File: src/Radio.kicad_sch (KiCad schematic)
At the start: 12 parts, among them J17 Line out, Q5 BPW96B

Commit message: Update Schematics design
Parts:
- removed Q5: BPW96B, LED_THT:LED_D5.0mm, symbol Device:Q_Photo_NPN
- renumbered J17 to J26
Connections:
- net GND: no longer J?.4 (Pin_4)
- net LightSensor: no longer names the net of J?.3 (Pin_3)
- new net GNDRadio: J?.4 (Pin_4)
- no-connect marks 0 -> 1
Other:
- note added: "Crashbar speakers"
- note added: "Handlebar speakers"
- note added: "Left Side Fork Column cover"
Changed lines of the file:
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@@
   (junction (at 255.27 111.76) (diameter 0) (color 0 0 0 0)
   )
-  (junction (at 142.24 85.09) (diameter 0) (color 0 0 0 0)
-  )
   (junction (at 97.79 76.2) (diameter 0) (color 0 0 0 0)
   )
-  (junction (at 129.54 67.31) (diameter 0) (color 0 0 0 0)
-  )
-  (wire (pts (xy 129.54 85.09) (xy 142.24 85.09))
-    (stroke (width 0) (type default))
-  )
+  (no_connect (at 142.24 67.31))
   (wire (pts (xy 238.76 116.84) (xy 228.6 116.84))
     (stroke (width 0) (type default) (color 72 72 72 1))
@@
     (stroke (width 0) (type default))
   )
-  (wire (pts (xy 142.24 69.85) (xy 142.24 85.09))
+  (wire (pts (xy 142.24 69.85) (xy 142.24 101.6))
     (stroke (width 0) (type default))
   )
@@
   )
   (wire (pts (xy 54.61 76.2) (xy 54.61 72.39))
-    (stroke (width 0) (type default))
-  )
-  (wire (pts (xy 142.24 85.09) (xy 142.24 101.6))
     (stroke (width 0) (type default))
   )
@@
     (stroke (width 0) (type default) (color 255 255 255 1))
   )
-  (wire (pts (xy 129.54 85.09) (xy 129.54 81.28))
-    (stroke (width 0) (type default))
-  )
   (wire (pts (xy 54.61 100.33) (xy 69.85 100.33))
     (stroke (width 0) (type default))
   )
-  (wire (pts (xy 125.73 67.31) (xy 129.54 67.31))
-    (stroke (width 0) (type default))
-  )
   (wire (pts (xy 144.78 137.16) (xy 147.32 137.16))
     (stroke (width 0) (type default))
@@
   )
   (wire (pts (xy 48.26 127) (xy 54.61 127))
-    (stroke (width 0) (type default))
-  )
-  (wire (pts (xy 129.54 67.31) (xy 142.24 67.31))
     (stroke (width 0) (type default))
   )
@@
     (stroke (width 0) (type default))
   )
-  (wire (pts (xy 129.54 71.12) (xy 129.54 67.31))
-    (stroke (width 0) (type default))
-  )
   (wire (pts (xy 246.38 105.41) (xy 228.6 105.41))
     (stroke (width 0) (type default))
@@
     (fill (type none))
   )
+  (rectangle (start 243.84 91.44) (end 267.97 146.05)
+    (stroke (width 0) (type default))
+    (fill (type none))
+  )
   (text "Speakers" (at 38.1 63.5 0)
+    (effects (font (size 1.27 1.27)) (justify left bottom))
+  )
+  (text "Handlebar speakers" (at 67.31 71.12 0)
+    (effects (font (size 1.27 1.27)) (justify left bottom))
+  )
+  (text "Left Side Fork Column cover" (at 243.84 148.59 0)
+    (effects (font (size 1.27 1.27)) (justify left bottom))
+  )
+  (text "Crashbar speakers" (at 67.31 133.35 0)
     (effects (font (size 1.27 1.27)) (justify left bottom))
   )
@@
     (effects (font (size 1.27 1.27)) (justify right))
     (property "Intersheetrefs" "${INTERSHEET_REFS}" (at 218.7168 102.87 0)
-      (effects (font (size 1.27 1.27)) (justify right) hide)
-    )
-  )
-  (global_label "LightSensor" (shape output) (at 125.73 67.31 180) (fields_autoplaced)
-    (effects (font (size 1.27 1.27)) (justify right))
-    (property "Intersheetrefs" "${INTERSHEET_REFS}" (at 111.7572 67.31 0)
       (effects (font (size 1.27 1.27)) (justify right) hide)
     )
@@
         )
         (path "/e63e39d7-6ac0-4ffd-8aa3-1841a4541b55/ddab4412-d22a-447e-a3b8-944a9a68a530"
-          (reference "J13") (unit 1)
-        )
-      )
-    )
-  )
-  (symbol (lib_id "power:GND") (at 176.53 101.6 90) (unit 1)
-    (in_bom yes) (on_board yes) (dnp no)
-    (property "Reference" "#PWR?" (at 182.88 101.6 0)
-      (effects (font (size 1.27 1.27)) hide)
-    )
-    (property "Value" "GND" (at 180.34 101.6 90)
-      (effects (font (size 1.27 1.27)) (justify right))
-    )
-    (property "Footprint" "" (at 176.53 101.6 0)
-      (effects (font (size 1.27 1.27)) hide)
-    )
-    (property "Datasheet" "" (at 176.53 101.6 0)
-      (effects (font (size 1.27 1.27)) hide)
-    )
-    (pin "1")
-    (instances
-      (project "dragstar-infotainment"
-        (path "/e63e39d7-6ac0-4ffd-8aa3-1841a4541b55"
-          (reference "#PWR?") (unit 1)
-        )
-        (path "/e63e39d7-6ac0-4ffd-8aa3-1841a4541b55/ddab4412-d22a-447e-a3b8-944a9a68a530"
-          (reference "#PWR068") (unit 1)
+          (reference "J22") (unit 1)
         )
       )
@@
         )
         (path "/e63e39d7-6ac0-4ffd-8aa3-1841a4541b55/ddab4412-d22a-447e-a3b8-944a9a68a530"
-          (reference "J15") (unit 1)
+          (reference "J24") (unit 1)
         )
       )
@@
         )
         (path "/e63e39d7-6ac0-4ffd-8aa3-1841a4541b55/ddab4412-d22a-447e-a3b8-944a9a68a530"
-          (reference "#PWR071") (unit 1)
+          (reference "#PWR074") (unit 1)
         )
       )
@@
         )
         (path "/e63e39d7-6ac0-4ffd-8aa3-1841a4541b55/ddab4412-d22a-447e-a3b8-944a9a68a530"
-          (reference "J11") (unit 1)
+          (reference "J20") (unit 1)
         )
       )
@@
         )
         (path "/e63e39d7-6ac0-4ffd-8aa3-1841a4541b55/ddab4412-d22a-447e-a3b8-944a9a68a530"
-          (reference "J14") (unit 1)
+          (reference "J23") (unit 1)
         )
       )
@@
         )
         (path "/e63e39d7-6ac0-4ffd-8aa3-1841a4541b55/ddab4412-d22a-447e-a3b8-944a9a68a530"
-          (reference "#PWR073") (unit 1)
+          (reference "#PWR076") (unit 1)
         )
       )
@@
         (path "/e63e39d7-6ac0-4ffd-8aa3-1841a4541b55/ddab4412-d22a-447e-a3b8-944a9a68a530"
           (reference "LS4") (unit 1)
+        )
+      )
+    )
+  )
+  (symbol (lib_id "Local Components:GNDRadio") (at 176.53 101.6 90) (unit 1)
+    (in_bom yes) (on_board yes) (dnp no) (fields_autoplaced)
+    (property "Reference" "#PWR021" (at 182.88 101.6 0)
+      (effects (font (size 1.27 1.27)) hide)
+    )
+    (property "Value" "GNDRadio" (at 180.34 102.235 90)
+      (effects (font (size 1.27 1.27)) (justify right))
+    )
+    (property "Footprint" "" (at 176.53 101.6 0)
+      (effects (font (size 1.27 1.27)) hide)
+    )
+    (property "Datasheet" "" (at 176.53 101.6 0)
+      (effects (font (size 1.27 1.27)) hide)
+    )
+    (pin "1")
+    (instances
+      (project "dragstar-infotainment"
+        (path "/e63e39d7-6ac0-4ffd-8aa3-1841a4541b55/5d40715c-dfc9-4b95-9cc7-adbd4b609d9b"
+          (reference "#PWR021") (unit 1)
+        )
+        (path "/e63e39d7-6ac0-4ffd-8aa3-1841a4541b55/ddab4412-d22a-447e-a3b8-944a9a68a530"
+          (reference "#PWR071") (unit 1)
         )
       )
@@
         )
         (path "/e63e39d7-6ac0-4ffd-8aa3-1841a4541b55/ddab4412-d22a-447e-a3b8-944a9a68a530"
-          (reference "J12") (unit 1)
+          (reference "J21") (unit 1)
         )
       )
@@
   (symbol (lib_id "Local Components:+5VRadio") (at 228.6 97.79 90) (unit 1)
     (in_bom yes) (on_board yes) (dnp no)
-    (property "Reference" "#PWR070" (at 232.41 97.79 0)
+    (property "Reference" "#PWR073" (at 232.41 97.79 0)
       (effects (font (size 1.27 1.27)) hide)
     )
@@
       (project "dragstar-infotainment"
         (path "/e63e39d7-6ac0-4ffd-8aa3-1841a4541b55/ddab4412-d22a-447e-a3b8-944a9a68a530"
-          (reference "#PWR070") (unit 1)
+          (reference "#PWR073") (unit 1)
         )
       )
@@
         )
         (path "/e63e39d7-6ac0-4ffd-8aa3-1841a4541b55/ddab4412-d22a-447e-a3b8-944a9a68a530"
-          (reference "#PWR072") (unit 1)
+          (reference "#PWR075") (unit 1)
         )
       )
@@
         )
         (path "/e63e39d7-6ac0-4ffd-8aa3-1841a4541b55/ddab4412-d22a-447e-a3b8-944a9a68a530"
-          (reference "#PWR069") (unit 1)
+          (reference "#PWR072") (unit 1)
         )
       )
@@
   (symbol (lib_id "Connector:Conn_Coaxial_x2") (at 255.27 119.38 0) (unit 1)
     (in_bom yes) (on_board yes) (dnp no) (fields_autoplaced)
-    (property "Reference" "J17" (at 257.81 119.0382 0)
+    (property "Reference" "J26" (at 257.81 119.0382 0)
       (effects (font (size 1.27 1.27)) (justify left))
     )
@@
       (project "dragstar-infotainment"
         (path "/e63e39d7-6ac0-4ffd-8aa3-1841a4541b55/ddab4412-d22a-447e-a3b8-944a9a68a530"
-          (reference "J17") (unit 1)
+          (reference "J26") (unit 1)
         )
       )
@@
         )
         (path "/e63e39d7-6ac0-4ffd-8aa3-1841a4541b55/ddab4412-d22a-447e-a3b8-944a9a68a530"
-          (reference "J16") (unit 1)
-        )
-      )
-    )
-  )
-  (symbol (lib_id "Device:Q_Photo_NPN") (at 127 76.2 0) (unit 1)
-    (in_bom yes) (on_board yes) (dnp no)
-    (property "Reference" "Q5" (at 132.08 74.8157 0)
-      (effects (font (size 1.27 1.27)) (justify left))
-    )
-    (property "Value" "BPW96B" (at 120.65 81.28 0)
-      (effects (font (size 1.27 1.27)) (justify left))
-    )
-    (property "Footprint" "LED_THT:LED_D5.0mm" (at 132.08 73.66 0)
-      (effects (font (size 1.27 1.27)) hide)
-    )
-    (property "Datasheet" "https://storage.googleapis.com/mauser-public-files/mauser.pt/catalog/userfiles/bpw96.pdf" (at 127 76.2 0)
-      (effects (font (size 1.27 1.27)) hide)
-    )
-    (property "Vendor" "Mauser" (at 127 76.2 0)
-      (effects (font (size 1.27 1.27)) hide)
-    )
-    (property "Vendor Link" "https://mauser.pt/catalog/product_info.php?products_id=017-0313" (at 127 76.2 0)
-      (effects (font (size 1.27 1.27)) hide)
-    )
-    (property "Vendor Ref" "017-0313" (at 127 76.2 0)
-      (effects (font (size 1.27 1.27)) hide)
-    )
-    (pin "1")
-    (pin "2")
-    (instances
-      (project "dragstar-infotainment"
-        (path "/e63e39d7-6ac0-4ffd-8aa3-1841a4541b55/ddab4412-d22a-447e-a3b8-944a9a68a530"
-          (reference "Q5") (unit 1)
+          (reference "J25") (unit 1)
         )
       )
@@
         )
         (path "/e63e39d7-6ac0-4ffd-8aa3-1841a4541b55/ddab4412-d22a-447e-a3b8-944a9a68a530"
-          (reference "#FLG012") (unit 1)
+          (reference "#FLG013") (unit 1)
         )
       )
@@
         )
         (path "/e63e39d7-6ac0-4ffd-8aa3-1841a4541b55/ddab4412-d22a-447e-a3b8-944a9a68a530"
-          (reference "#PWR067") (unit 1)
-        )
-      )
+          (reference "#PWR070") (unit 1)
+        )
+      )

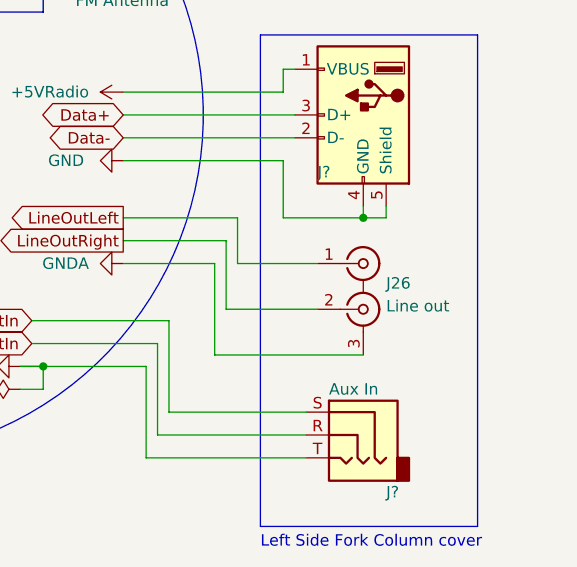
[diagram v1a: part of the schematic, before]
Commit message: Add radio backup battery circuit; Update cable harness; rework main board circuit
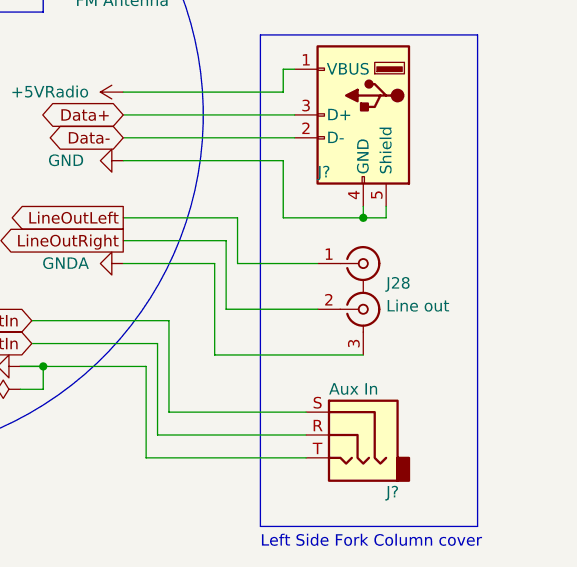
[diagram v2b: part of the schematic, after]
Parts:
- renumbered J26 to J28
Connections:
- net VRadio: no longer J?.1 (VBUS)
- new net +5VRadio: J?.1 (VBUS)
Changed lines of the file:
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@@
   )
   (wire (pts (xy 246.38 97.79) (xy 246.38 95.25))
-    (stroke (width 0) (type default) (color 255 0 0 1))
+    (stroke (width 0) (type default))
   )
   (wire (pts (xy 97.79 127) (xy 104.14 127))
@@
   )
   (wire (pts (xy 246.38 95.25) (xy 247.65 95.25))
-    (stroke (width 0) (type default) (color 255 0 0 1))
+    (stroke (width 0) (type default))
   )
   (wire (pts (xy 238.76 127) (xy 238.76 116.84))
@@
   )
   (wire (pts (xy 228.6 97.79) (xy 246.38 97.79))
-    (stroke (width 0) (type default) (color 255 0 0 1))
+    (stroke (width 0) (type default))
   )
   (wire (pts (xy 95.25 76.2) (xy 88.9 76.2))
@@
         )
         (path "/e63e39d7-6ac0-4ffd-8aa3-1841a4541b55/ddab4412-d22a-447e-a3b8-944a9a68a530"
-          (reference "J22") (unit 1)
+          (reference "J24") (unit 1)
         )
       )
@@
         )
         (path "/e63e39d7-6ac0-4ffd-8aa3-1841a4541b55/ddab4412-d22a-447e-a3b8-944a9a68a530"
-          (reference "J24") (unit 1)
+          (reference "J26") (unit 1)
         )
       )
@@
         )
         (path "/e63e39d7-6ac0-4ffd-8aa3-1841a4541b55/ddab4412-d22a-447e-a3b8-944a9a68a530"
-          (reference "#PWR074") (unit 1)
+          (reference "#PWR075") (unit 1)
         )
       )
@@
         )
         (path "/e63e39d7-6ac0-4ffd-8aa3-1841a4541b55/ddab4412-d22a-447e-a3b8-944a9a68a530"
-          (reference "J20") (unit 1)
+          (reference "J22") (unit 1)
         )
       )
@@
         )
         (path "/e63e39d7-6ac0-4ffd-8aa3-1841a4541b55/ddab4412-d22a-447e-a3b8-944a9a68a530"
-          (reference "J23") (unit 1)
+          (reference "J25") (unit 1)
         )
       )
@@
         )
         (path "/e63e39d7-6ac0-4ffd-8aa3-1841a4541b55/ddab4412-d22a-447e-a3b8-944a9a68a530"
-          (reference "#PWR076") (unit 1)
+          (reference "#PWR077") (unit 1)
         )
       )
@@
   (symbol (lib_id "Local Components:GNDRadio") (at 176.53 101.6 90) (unit 1)
     (in_bom yes) (on_board yes) (dnp no) (fields_autoplaced)
-    (property "Reference" "#PWR021" (at 182.88 101.6 0)
+    (property "Reference" "#PWR?" (at 182.88 101.6 0)
       (effects (font (size 1.27 1.27)) hide)
     )
@@
       (project "dragstar-infotainment"
         (path "/e63e39d7-6ac0-4ffd-8aa3-1841a4541b55/5d40715c-dfc9-4b95-9cc7-adbd4b609d9b"
-          (reference "#PWR021") (unit 1)
-        )
-        (path "/e63e39d7-6ac0-4ffd-8aa3-1841a4541b55/ddab4412-d22a-447e-a3b8-944a9a68a530"
-          (reference "#PWR071") (unit 1)
+          (reference "#PWR?") (unit 1)
+        )
+        (path "/e63e39d7-6ac0-4ffd-8aa3-1841a4541b55/ddab4412-d22a-447e-a3b8-944a9a68a530"
+          (reference "#PWR072") (unit 1)
+        )
+      )
+    )
+  )
+  (symbol (lib_id "Local Components:+5VRadio") (at 228.6 97.79 90) (unit 1)
+    (in_bom yes) (on_board yes) (dnp no)
+    (property "Reference" "#PWR074" (at 232.41 97.79 0)
+      (effects (font (size 1.27 1.27)) hide)
+    )
+    (property "Value" "+5VRadio" (at 224.79 97.79 90)
+      (effects (font (size 1.27 1.27)) (justify left))
+    )
+    (property "Footprint" "" (at 228.6 97.79 0)
+      (effects (font (size 1.27 1.27)) hide)
+    )
+    (property "Datasheet" "" (at 228.6 97.79 0)
+      (effects (font (size 1.27 1.27)) hide)
+    )
+    (pin "1")
+    (instances
+      (project "dragstar-infotainment"
+        (path "/e63e39d7-6ac0-4ffd-8aa3-1841a4541b55/ddab4412-d22a-447e-a3b8-944a9a68a530"
+          (reference "#PWR074") (unit 1)
         )
       )
@@
         )
         (path "/e63e39d7-6ac0-4ffd-8aa3-1841a4541b55/ddab4412-d22a-447e-a3b8-944a9a68a530"
-          (reference "J21") (unit 1)
-        )
-      )
-    )
-  )
-  (symbol (lib_id "Local Components:+5VRadio") (at 228.6 97.79 90) (unit 1)
-    (in_bom yes) (on_board yes) (dnp no)
-    (property "Reference" "#PWR073" (at 232.41 97.79 0)
-      (effects (font (size 1.27 1.27)) hide)
-    )
-    (property "Value" "+5VRadio" (at 224.79 97.79 90)
-      (effects (font (size 1.27 1.27)) (justify left))
-    )
-    (property "Footprint" "" (at 228.6 97.79 0)
-      (effects (font (size 1.27 1.27)) hide)
-    )
-    (property "Datasheet" "" (at 228.6 97.79 0)
-      (effects (font (size 1.27 1.27)) hide)
-    )
-    (pin "1")
-    (instances
-      (project "dragstar-infotainment"
-        (path "/e63e39d7-6ac0-4ffd-8aa3-1841a4541b55/ddab4412-d22a-447e-a3b8-944a9a68a530"
-          (reference "#PWR073") (unit 1)
+          (reference "J23") (unit 1)
         )
       )
@@
         )
         (path "/e63e39d7-6ac0-4ffd-8aa3-1841a4541b55/ddab4412-d22a-447e-a3b8-944a9a68a530"
-          (reference "#PWR075") (unit 1)
+          (reference "#PWR076") (unit 1)
         )
       )
@@
         )
         (path "/e63e39d7-6ac0-4ffd-8aa3-1841a4541b55/ddab4412-d22a-447e-a3b8-944a9a68a530"
-          (reference "#PWR072") (unit 1)
+          (reference "#PWR073") (unit 1)
         )
       )
@@
   (symbol (lib_id "Connector:Conn_Coaxial_x2") (at 255.27 119.38 0) (unit 1)
     (in_bom yes) (on_board yes) (dnp no) (fields_autoplaced)
-    (property "Reference" "J26" (at 257.81 119.0382 0)
+    (property "Reference" "J28" (at 257.81 119.0382 0)
       (effects (font (size 1.27 1.27)) (justify left))
     )
@@
       (project "dragstar-infotainment"
         (path "/e63e39d7-6ac0-4ffd-8aa3-1841a4541b55/ddab4412-d22a-447e-a3b8-944a9a68a530"
-          (reference "J26") (unit 1)
+          (reference "J28") (unit 1)
         )
       )
@@
         )
         (path "/e63e39d7-6ac0-4ffd-8aa3-1841a4541b55/ddab4412-d22a-447e-a3b8-944a9a68a530"
-          (reference "J25") (unit 1)
+          (reference "J27") (unit 1)
         )
       )
@@
         )
         (path "/e63e39d7-6ac0-4ffd-8aa3-1841a4541b55/ddab4412-d22a-447e-a3b8-944a9a68a530"
-          (reference "#FLG013") (unit 1)
+          (reference "#FLG012") (unit 1)
         )
       )
@@
         )
         (path "/e63e39d7-6ac0-4ffd-8aa3-1841a4541b55/ddab4412-d22a-447e-a3b8-944a9a68a530"
-          (reference "#PWR070") (unit 1)
-        )
-      )
+          (reference "#PWR071") (unit 1)
+        )
+      )

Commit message: update Schematics
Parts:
- removed J28: Line out, symbol Connector:Conn_Coaxial_x2
- added AE1: Antenna_Shield, symbol Device:Antenna_Shield
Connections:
- net GNDRadio is gone; now on net GND: J?.4 (Pin_4)
- net GND: now also AE1.2 (Shield)
- net Ant: no longer names the net of J?.1 (In)
- net Ant: now also AE1.1 (A)
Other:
- moved on the sheet: J?

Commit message: Update Schmatics; Cleanup unecessary circuits; Simplify blinkers dimmers; Update PCB; Colorize motorcycle electric diagram.
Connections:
- net Killswitch renamed Key
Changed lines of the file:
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@@
     )
   )
-  (global_label "Killswitch" (shape output) (at 177.8 96.52 0) (fields_autoplaced)
+  (global_label "Key" (shape output) (at 177.8 96.52 0) (fields_autoplaced)
     (effects (font (size 1.27 1.27)) (justify left))
-    (property "Intersheetrefs" "${INTERSHEET_REFS}" (at 189.8377 96.52 0)
+    (property "Intersheetrefs" "${INTERSHEET_REFS}" (at 184.032 96.52 0)
       (effects (font (size 1.27 1.27)) (justify left) hide)
     )
@@
         )
         (path "/e63e39d7-6ac0-4ffd-8aa3-1841a4541b55/ddab4412-d22a-447e-a3b8-944a9a68a530"
-          (reference "J13") (unit 1)
+          (reference "J47") (unit 1)
         )
       )
@@
         )
         (path "/e63e39d7-6ac0-4ffd-8aa3-1841a4541b55/ddab4412-d22a-447e-a3b8-944a9a68a530"
-          (reference "J12") (unit 1)
+          (reference "J49") (unit 1)
         )
       )
@@
         )
         (path "/e63e39d7-6ac0-4ffd-8aa3-1841a4541b55/ddab4412-d22a-447e-a3b8-944a9a68a530"
-          (reference "LS1") (unit 1)
+          (reference "LS2") (unit 1)
         )
       )
@@
         )
         (path "/e63e39d7-6ac0-4ffd-8aa3-1841a4541b55/ddab4412-d22a-447e-a3b8-944a9a68a530"
-          (reference "#PWR058") (unit 1)
+          (reference "#PWR070") (unit 1)
         )
       )
@@
         )
         (path "/e63e39d7-6ac0-4ffd-8aa3-1841a4541b55/ddab4412-d22a-447e-a3b8-944a9a68a530"
-          (reference "#FLG010") (unit 1)
+          (reference "#FLG011") (unit 1)
         )
       )
@@
         )
         (path "/e63e39d7-6ac0-4ffd-8aa3-1841a4541b55/ddab4412-d22a-447e-a3b8-944a9a68a530"
-          (reference "J10") (unit 1)
+          (reference "J45") (unit 1)
         )
       )
@@
         )
         (path "/e63e39d7-6ac0-4ffd-8aa3-1841a4541b55/ddab4412-d22a-447e-a3b8-944a9a68a530"
-          (reference "J9") (unit 1)
+          (reference "J48") (unit 1)
         )
       )
@@
         )
         (path "/e63e39d7-6ac0-4ffd-8aa3-1841a4541b55/ddab4412-d22a-447e-a3b8-944a9a68a530"
-          (reference "#PWR054") (unit 1)
+          (reference "#PWR071") (unit 1)
         )
       )
@@
         )
         (path "/e63e39d7-6ac0-4ffd-8aa3-1841a4541b55/ddab4412-d22a-447e-a3b8-944a9a68a530"
-          (reference "LS3") (unit 1)
+          (reference "LS1") (unit 1)
         )
       )
@@
   (symbol (lib_id "Local Components:+5VRadio") (at 228.6 97.79 90) (unit 1)
     (in_bom yes) (on_board yes) (dnp no)
-    (property "Reference" "#PWR055" (at 232.41 97.79 0)
+    (property "Reference" "#PWR069" (at 232.41 97.79 0)
       (effects (font (size 1.27 1.27)) hide)
     )
@@
       (project "dragstar-infotainment"
         (path "/e63e39d7-6ac0-4ffd-8aa3-1841a4541b55/ddab4412-d22a-447e-a3b8-944a9a68a530"
-          (reference "#PWR055") (unit 1)
+          (reference "#PWR069") (unit 1)
         )
       )
@@
         )
         (path "/e63e39d7-6ac0-4ffd-8aa3-1841a4541b55/ddab4412-d22a-447e-a3b8-944a9a68a530"
-          (reference "J8") (unit 1)
+          (reference "J46") (unit 1)
         )
       )
@@
         )
         (path "/e63e39d7-6ac0-4ffd-8aa3-1841a4541b55/ddab4412-d22a-447e-a3b8-944a9a68a530"
-          (reference "#PWR059") (unit 1)
+          (reference "#PWR068") (unit 1)
         )
       )
@@
         )
         (path "/e63e39d7-6ac0-4ffd-8aa3-1841a4541b55/ddab4412-d22a-447e-a3b8-944a9a68a530"
-          (reference "J11") (unit 1)
+          (reference "J50") (unit 1)
         )
       )
@@
   (symbol (lib_id "power:GND") (at 176.53 101.6 90) (unit 1)
     (in_bom yes) (on_board yes) (dnp no)
-    (property "Reference" "#PWR057" (at 182.88 101.6 0)
+    (property "Reference" "#PWR067" (at 182.88 101.6 0)
       (effects (font (size 1.27 1.27)) hide)
     )
@@
       (project "dragstar-infotainment"
         (path "/e63e39d7-6ac0-4ffd-8aa3-1841a4541b55/ddab4412-d22a-447e-a3b8-944a9a68a530"
-          (reference "#PWR057") (unit 1)
+          (reference "#PWR067") (unit 1)
         )
       )
@@
         )
         (path "/e63e39d7-6ac0-4ffd-8aa3-1841a4541b55/ddab4412-d22a-447e-a3b8-944a9a68a530"
-          (reference "LS2") (unit 1)
+          (reference "LS3") (unit 1)
         )
       )
@@
         )
         (path "/e63e39d7-6ac0-4ffd-8aa3-1841a4541b55/ddab4412-d22a-447e-a3b8-944a9a68a530"
-          (reference "#FLG011") (unit 1)
+          (reference "#FLG010") (unit 1)
         )
       )
@@
         )
         (path "/e63e39d7-6ac0-4ffd-8aa3-1841a4541b55/ddab4412-d22a-447e-a3b8-944a9a68a530"
-          (reference "#PWR056") (unit 1)
-        )
-      )
+          (reference "#PWR066") (unit 1)
+        )
+      )
